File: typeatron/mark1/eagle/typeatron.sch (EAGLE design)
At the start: 25 parts

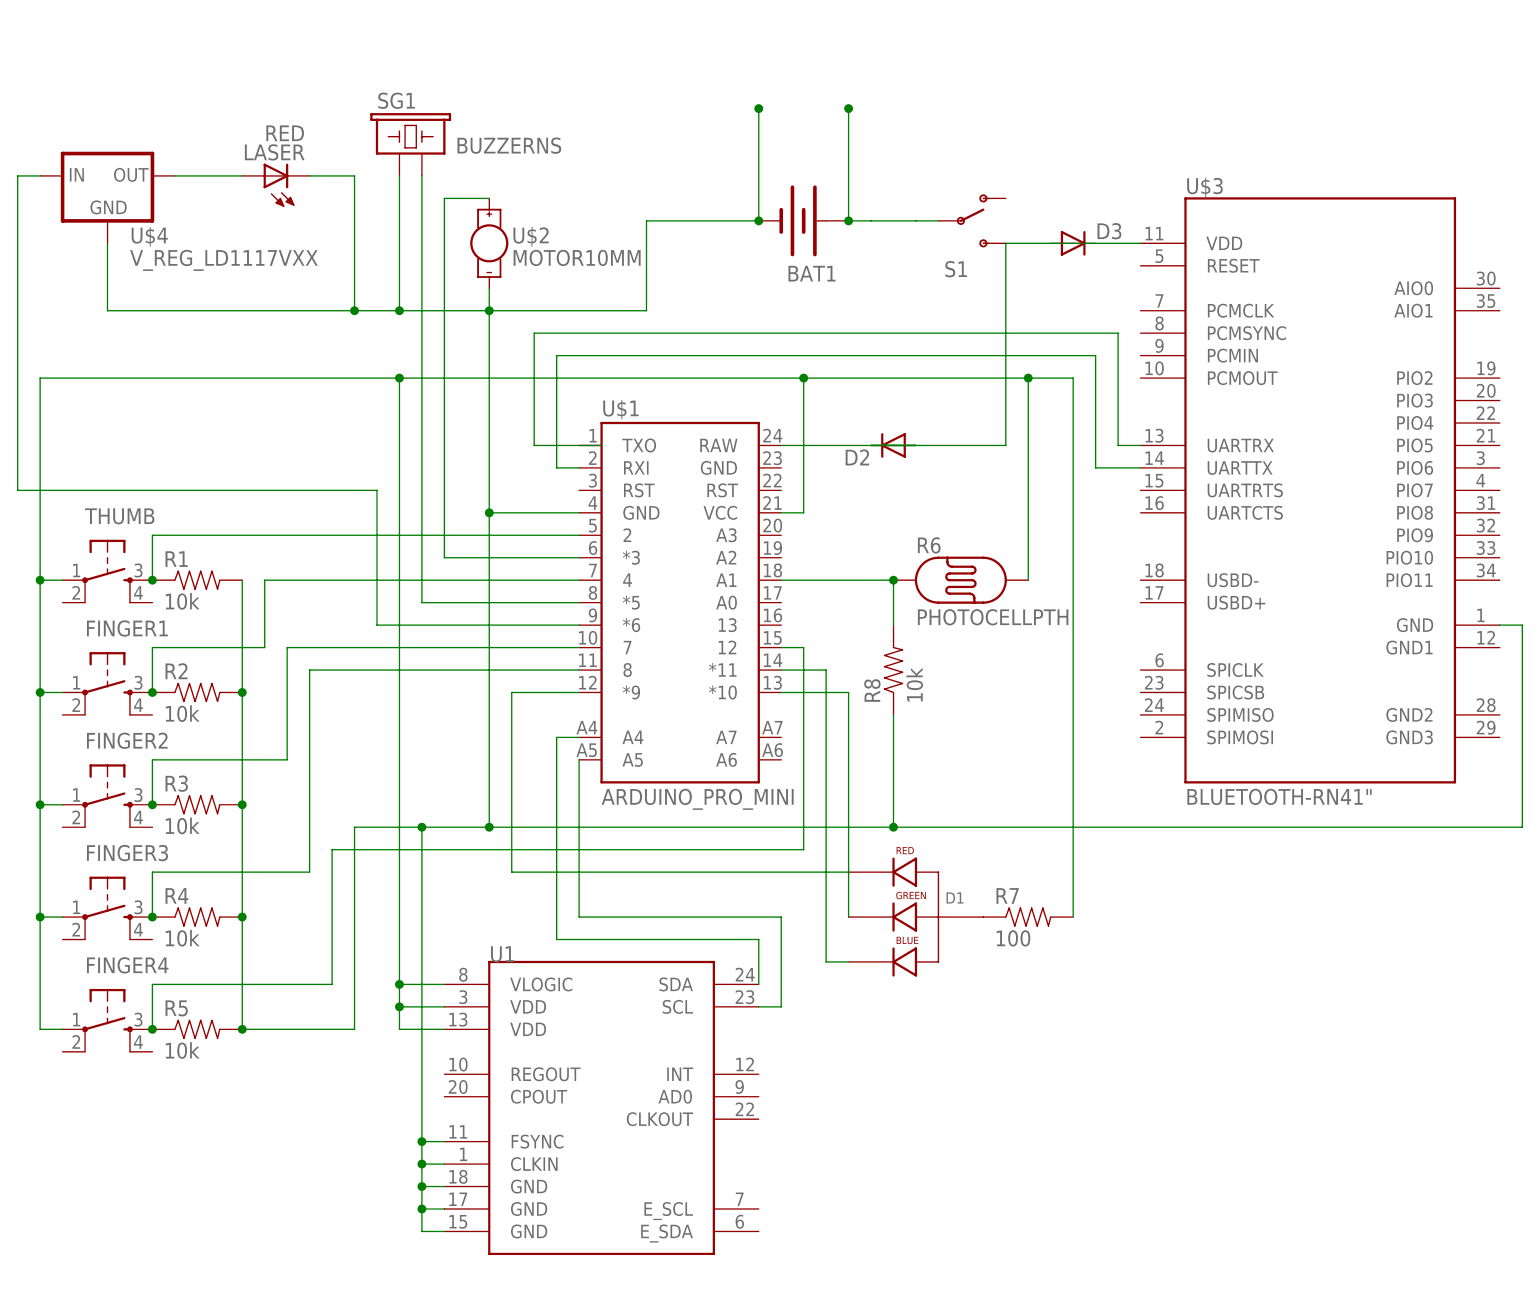
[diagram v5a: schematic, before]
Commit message: Removed the voltage regulator from the Typetron's laser, as the laser becomes too dim when on battery power. Connected both laser and Bluetooth modem to a ground line which is disconnected with a jumper when programming the Typeatron (to avoid frying the laser and confusing the microcontroller)
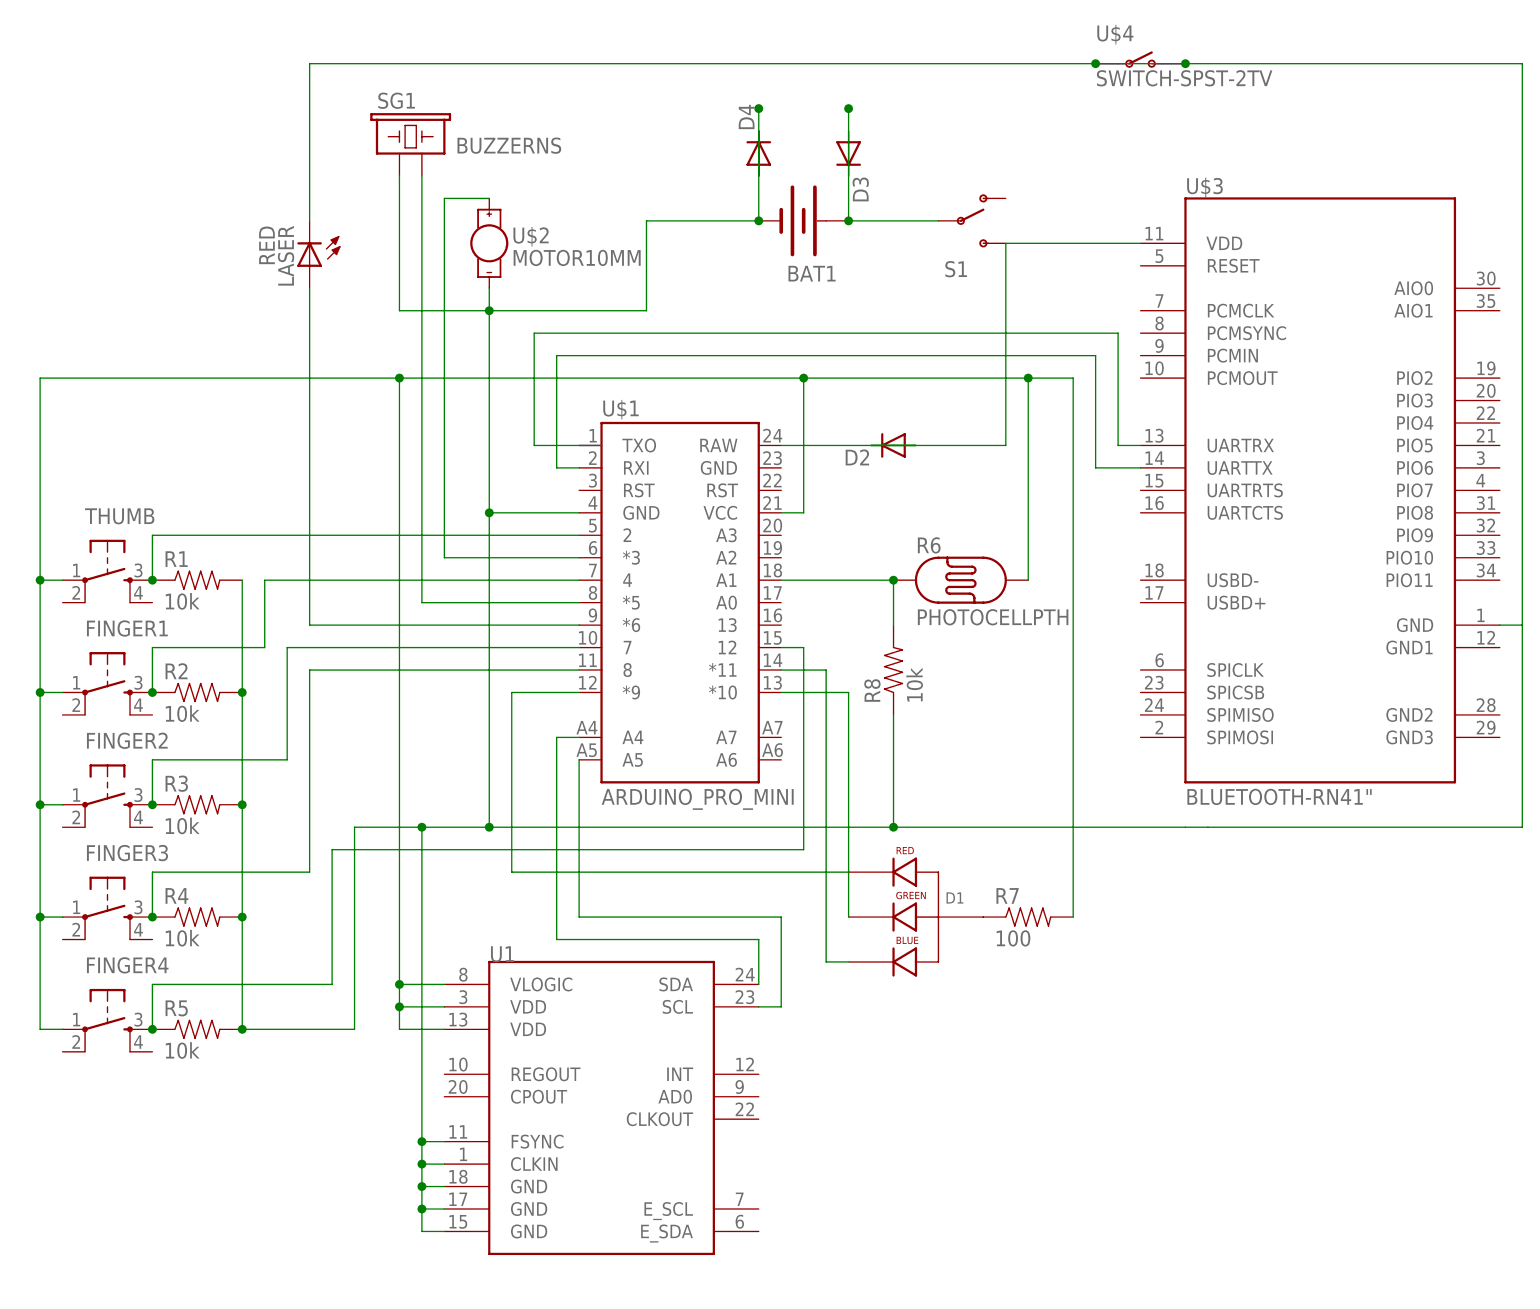
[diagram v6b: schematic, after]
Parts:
- added D4: (no value), SparkFun-DiscreteSemi:DIODEPTH
- U$4: value V_REG_LD1117VXX -> SWITCH-SPST-2TV; device SparkFun-PowerIC:V_REG_LD1117VXX -> SparkFun-Electromechanical:SWITCH-SPST-2TV
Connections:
- removed net N$24: U$1.*6, U$4.IN
- new net N$18: LASER.A
- net N$10: no longer D3.A, D3.C
- net N$19: now also U$1.*6; no longer LASER.A, U$4.OUT
- net N$3: now also D4.A, D4.C, U$4.O, U$4.P; no longer U$4.GND
- net N$9: now also D3.A, D3.C
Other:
- moved on the sheet: D3, LASER
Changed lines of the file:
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@@
 <part name="R8" library="SparkFun-Resistors" deviceset="10KOHM1/6W5%(PTH)" device="KIT" value="10k"/>
 <part name="D2" library="SparkFun-DiscreteSemi" deviceset="DIODE" device="PTH"/>
+<part name="LASER" library="SparkFun-LED" deviceset="LED-RED" device="0603" value="RED"/>
 <part name="D3" library="SparkFun-DiscreteSemi" deviceset="DIODE" device="PTH"/>
-<part name="U$4" library="SparkFun-PowerIC" deviceset="V_REG_LD1117VXX" device=""/>
-<part name="LASER" library="SparkFun-LED" deviceset="LED-RED" device="0603" value="RED"/>
+<part name="D4" library="SparkFun-DiscreteSemi" deviceset="DIODE" device="PTH"/>
+<part name="U$4" library="SparkFun-Electromechanical" deviceset="SWITCH-SPST-2" device="TV"/>
 </parts>
 <sheets>
@@
 <instance part="R8" gate="G$1" x="86.36" y="55.88" rot="R90"/>
 <instance part="D2" gate="G$1" x="86.36" y="81.28" rot="R180"/>
-<instance part="D3" gate="G$1" x="106.68" y="104.14"/>
-<instance part="U$4" gate="G$1" x="-2.54" y="111.76"/>
-<instance part="LASER" gate="G$1" x="15.24" y="111.76" rot="R90"/>
+<instance part="LASER" gate="G$1" x="20.32" y="101.6" rot="R180"/>
+<instance part="D3" gate="G$1" x="81.28" y="114.3" rot="R270"/>
+<instance part="D4" gate="G$1" x="71.12" y="114.3" rot="R90"/>
+<instance part="U$4" gate="G$1" x="114.3" y="124.46"/>
 </instances>
 <busses>
@@
 <pinref part="BAT1" gate="G$1" pin="+"/>
 <pinref part="S1" gate="1" pin="P"/>
-<wire x1="83.82" y1="106.68" x2="81.28" y2="106.68" width="0.1524" layer="91"/>
-<wire x1="81.28" y1="119.38" x2="81.28" y2="106.68" width="0.1524" layer="91"/>
+<wire x1="81.28" y1="119.38" x2="81.28" y2="116.84" width="0.1524" layer="91"/>
 <junction x="81.28" y="106.68"/>
-<wire x1="83.82" y1="106.68" x2="88.9" y2="106.68" width="0.1524" layer="91"/>
-<wire x1="88.9" y1="106.68" x2="91.44" y2="106.68" width="0.1524" layer="91"/>
+<wire x1="81.28" y1="116.84" x2="81.28" y2="111.76" width="0.1524" layer="91"/>
+<wire x1="81.28" y1="111.76" x2="81.28" y2="106.68" width="0.1524" layer="91"/>
+<wire x1="81.28" y1="106.68" x2="91.44" y2="106.68" width="0.1524" layer="91"/>
 <junction x="81.28" y="119.38"/>
+<pinref part="D3" gate="G$1" pin="A"/>
+<pinref part="D3" gate="G$1" pin="C"/>
 </segment>
 </net>
@@
 <wire x1="83.82" y1="81.28" x2="99.06" y2="81.28" width="0.1524" layer="91"/>
 <wire x1="99.06" y1="81.28" x2="99.06" y2="104.14" width="0.1524" layer="91"/>
-<wire x1="99.06" y1="104.14" x2="104.14" y2="104.14" width="0.1524" layer="91"/>
 <pinref part="U$3" gate="G$1" pin="VDD"/>
 <pinref part="D2" gate="G$1" pin="A"/>
 <pinref part="D2" gate="G$1" pin="C"/>
-<pinref part="D3" gate="G$1" pin="A"/>
-<wire x1="104.14" y1="104.14" x2="109.22" y2="104.14" width="0.1524" layer="91"/>
-<pinref part="D3" gate="G$1" pin="C"/>
-<wire x1="109.22" y1="104.14" x2="114.3" y2="104.14" width="0.1524" layer="91"/>
+<wire x1="99.06" y1="104.14" x2="114.3" y2="104.14" width="0.1524" layer="91"/>
 </segment>
 </net>
@@
 <pinref part="U$1" gate="G$1" pin="A4"/>
 <wire x1="48.26" y1="48.26" x2="50.8" y2="48.26" width="0.1524" layer="91"/>
+</segment>
+</net>
+<net name="N$19" class="0">
+<segment>
+<pinref part="U$1" gate="G$1" pin="*6"/>
+<wire x1="20.32" y1="60.96" x2="50.8" y2="60.96" width="0.1524" layer="91"/>
 </segment>
 </net>
@@
 <wire x1="40.64" y1="73.66" x2="40.64" y2="38.1" width="0.1524" layer="91"/>
 <wire x1="33.02" y1="2.54" x2="33.02" y2="38.1" width="0.1524" layer="91"/>
-<wire x1="86.36" y1="38.1" x2="157.48" y2="38.1" width="0.1524" layer="91"/>
+<wire x1="86.36" y1="38.1" x2="119.38" y2="38.1" width="0.1524" layer="91"/>
 <pinref part="SG1" gate="G$1" pin="1"/>
 <wire x1="30.48" y1="111.76" x2="30.48" y2="96.52" width="0.1524" layer="91"/>
@@
 <wire x1="40.64" y1="96.52" x2="58.42" y2="96.52" width="0.1524" layer="91"/>
 <pinref part="BAT1" gate="G$1" pin="-"/>
-<wire x1="71.12" y1="119.38" x2="71.12" y2="106.68" width="0.1524" layer="91"/>
+<wire x1="71.12" y1="119.38" x2="71.12" y2="111.76" width="0.1524" layer="91"/>
 <junction x="71.12" y="106.68"/>
+<wire x1="71.12" y1="111.76" x2="71.12" y2="116.84" width="0.1524" layer="91"/>
+<wire x1="71.12" y1="116.84" x2="71.12" y2="106.68" width="0.1524" layer="91"/>
 <wire x1="71.12" y1="106.68" x2="58.42" y2="106.68" width="0.1524" layer="91"/>
 <wire x1="58.42" y1="96.52" x2="58.42" y2="106.68" width="0.1524" layer="91"/>
 <junction x="40.64" y="96.52"/>
-<wire x1="157.48" y1="38.1" x2="157.48" y2="60.96" width="0.1524" layer="91"/>
-<pinref part="U$3" gate="G$1" pin="GND"/>
-<wire x1="157.48" y1="60.96" x2="154.94" y2="60.96" width="0.1524" layer="91"/>
 <wire x1="33.02" y1="38.1" x2="25.4" y2="38.1" width="0.1524" layer="91"/>
 <wire x1="25.4" y1="38.1" x2="25.4" y2="15.24" width="0.1524" layer="91"/>
@@
 <junction x="12.7" y="15.24"/>
 <junction x="71.12" y="119.38"/>
-<pinref part="LASER" gate="G$1" pin="C"/>
-<wire x1="20.32" y1="111.76" x2="25.4" y2="111.76" width="0.1524" layer="91"/>
-<wire x1="25.4" y1="111.76" x2="25.4" y2="96.52" width="0.1524" layer="91"/>
-<wire x1="25.4" y1="96.52" x2="30.48" y2="96.52" width="0.1524" layer="91"/>
-<junction x="30.48" y="96.52"/>
-<pinref part="U$4" gate="G$1" pin="GND"/>
-<wire x1="-2.54" y1="104.14" x2="-2.54" y2="96.52" width="0.1524" layer="91"/>
-<wire x1="-2.54" y1="96.52" x2="25.4" y2="96.52" width="0.1524" layer="91"/>
-<junction x="25.4" y="96.52"/>
 <pinref part="U$1" gate="G$1" pin="GND"/>
 <wire x1="50.8" y1="73.66" x2="40.64" y2="73.66" width="0.1524" layer="91"/>
 <junction x="40.64" y="73.66"/>
-</segment>
-</net>
-<net name="N$19" class="0">
-<segment>
-<pinref part="U$4" gate="G$1" pin="OUT"/>
+<pinref part="D4" gate="G$1" pin="A"/>
+<pinref part="D4" gate="G$1" pin="C"/>
+<pinref part="U$3" gate="G$1" pin="GND"/>
+<wire x1="119.38" y1="38.1" x2="121.92" y2="38.1" width="0.1524" layer="91"/>
+<wire x1="121.92" y1="38.1" x2="157.48" y2="38.1" width="0.1524" layer="91"/>
+<wire x1="157.48" y1="38.1" x2="157.48" y2="60.96" width="0.1524" layer="91"/>
+<wire x1="157.48" y1="60.96" x2="154.94" y2="60.96" width="0.1524" layer="91"/>
+<pinref part="LASER" gate="G$1" pin="C"/>
+<wire x1="20.32" y1="106.68" x2="20.32" y2="124.46" width="0.1524" layer="91"/>
+<wire x1="20.32" y1="124.46" x2="109.22" y2="124.46" width="0.1524" layer="91"/>
+<wire x1="109.22" y1="124.46" x2="119.38" y2="124.46" width="0.1524" layer="91"/>
+<wire x1="119.38" y1="124.46" x2="157.48" y2="124.46" width="0.1524" layer="91"/>
+<wire x1="157.48" y1="124.46" x2="157.48" y2="60.96" width="0.1524" layer="91"/>
+<pinref part="U$4" gate="G$1" pin="P"/>
+<junction x="109.22" y="124.46"/>
+<pinref part="U$4" gate="G$1" pin="O"/>
+<junction x="119.38" y="124.46"/>
+</segment>
+</net>
+<net name="N$18" class="0">
+<segment>
 <pinref part="LASER" gate="G$1" pin="A"/>
-<wire x1="5.08" y1="111.76" x2="12.7" y2="111.76" width="0.1524" layer="91"/>
-</segment>
-</net>
-<net name="N$24" class="0">
-<segment>
-<pinref part="U$4" gate="G$1" pin="IN"/>
-<wire x1="-10.16" y1="111.76" x2="-12.7" y2="111.76" width="0.1524" layer="91"/>
-<wire x1="-12.7" y1="111.76" x2="-12.7" y2="76.2" width="0.1524" layer="91"/>
-<wire x1="-12.7" y1="76.2" x2="27.94" y2="76.2" width="0.1524" layer="91"/>
-<wire x1="27.94" y1="76.2" x2="27.94" y2="60.96" width="0.1524" layer="91"/>
-<pinref part="U$1" gate="G$1" pin="*6"/>
-<wire x1="27.94" y1="60.96" x2="50.8" y2="60.96" width="0.1524" layer="91"/>
-</segment>
-</net>
+<wire x1="20.32" y1="60.96" x2="20.32" y2="99.06" width="0.1524" layer="91"/>
+</segment>
+</net>
